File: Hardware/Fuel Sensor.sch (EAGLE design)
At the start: 30 parts, among them IC1 LP2950ACZ-3.3G (TO92), IC2 LTV814, IC3 2N5551, K1 FINDER34-SPDT5, M0 HLK-PM01-AC-DC, M1 WIRELESS-NRF24L01BIG, M2 ARDUINO-PRO-MINI-2ROWSBIG, X1 220Vac, X2 Relay

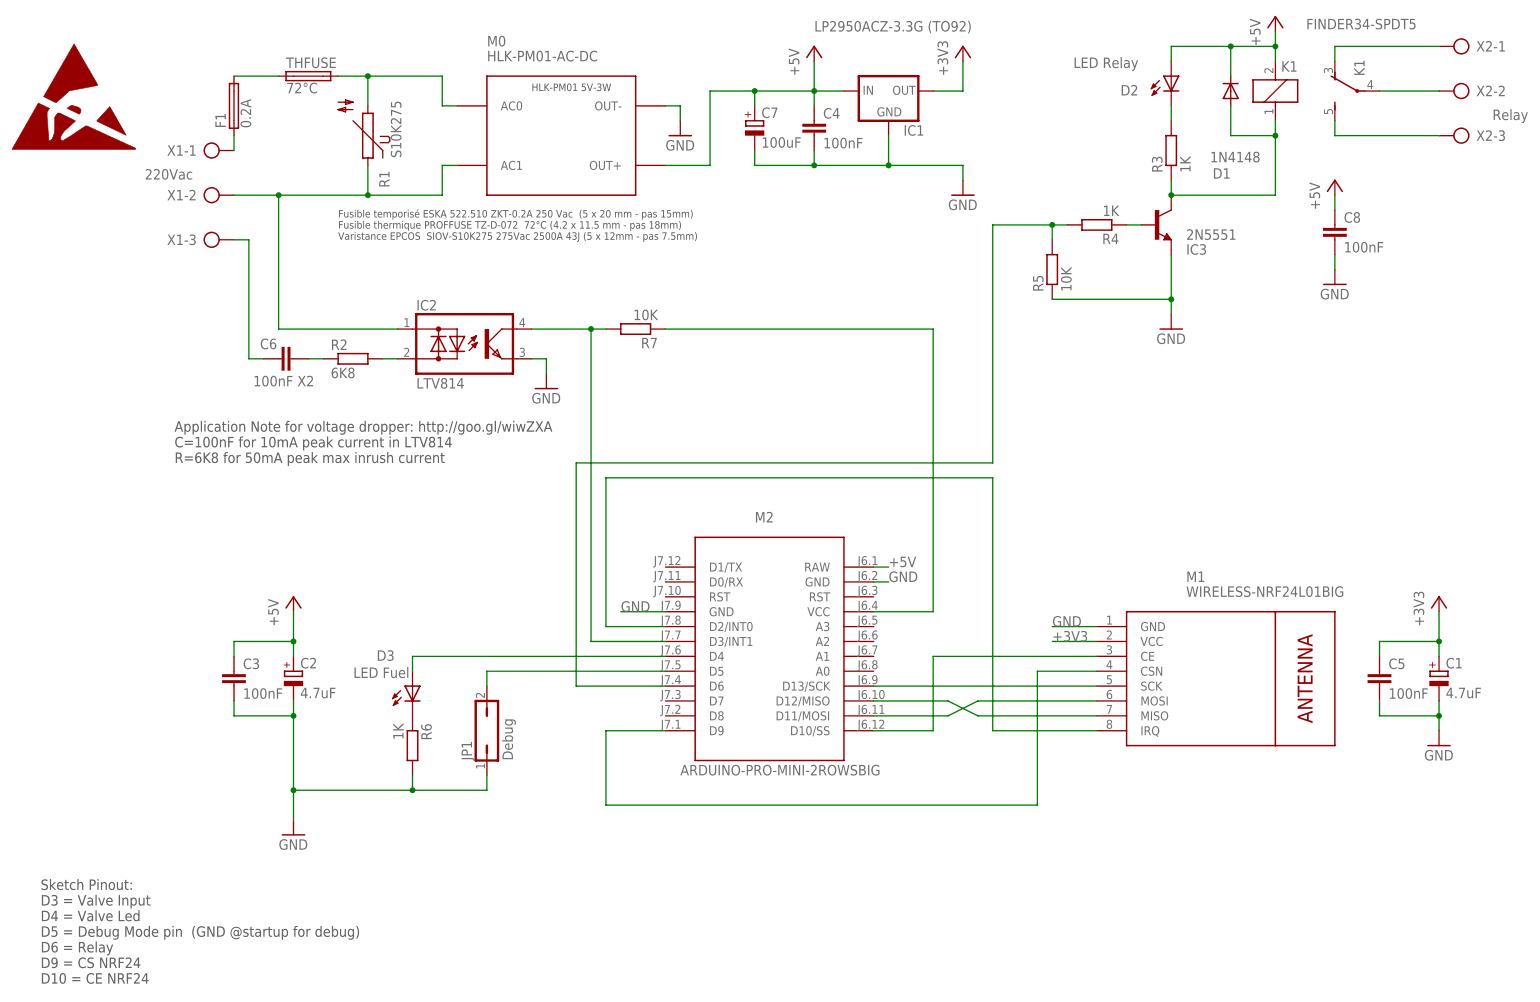
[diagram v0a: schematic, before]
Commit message: Fix Resistor values for LEDs
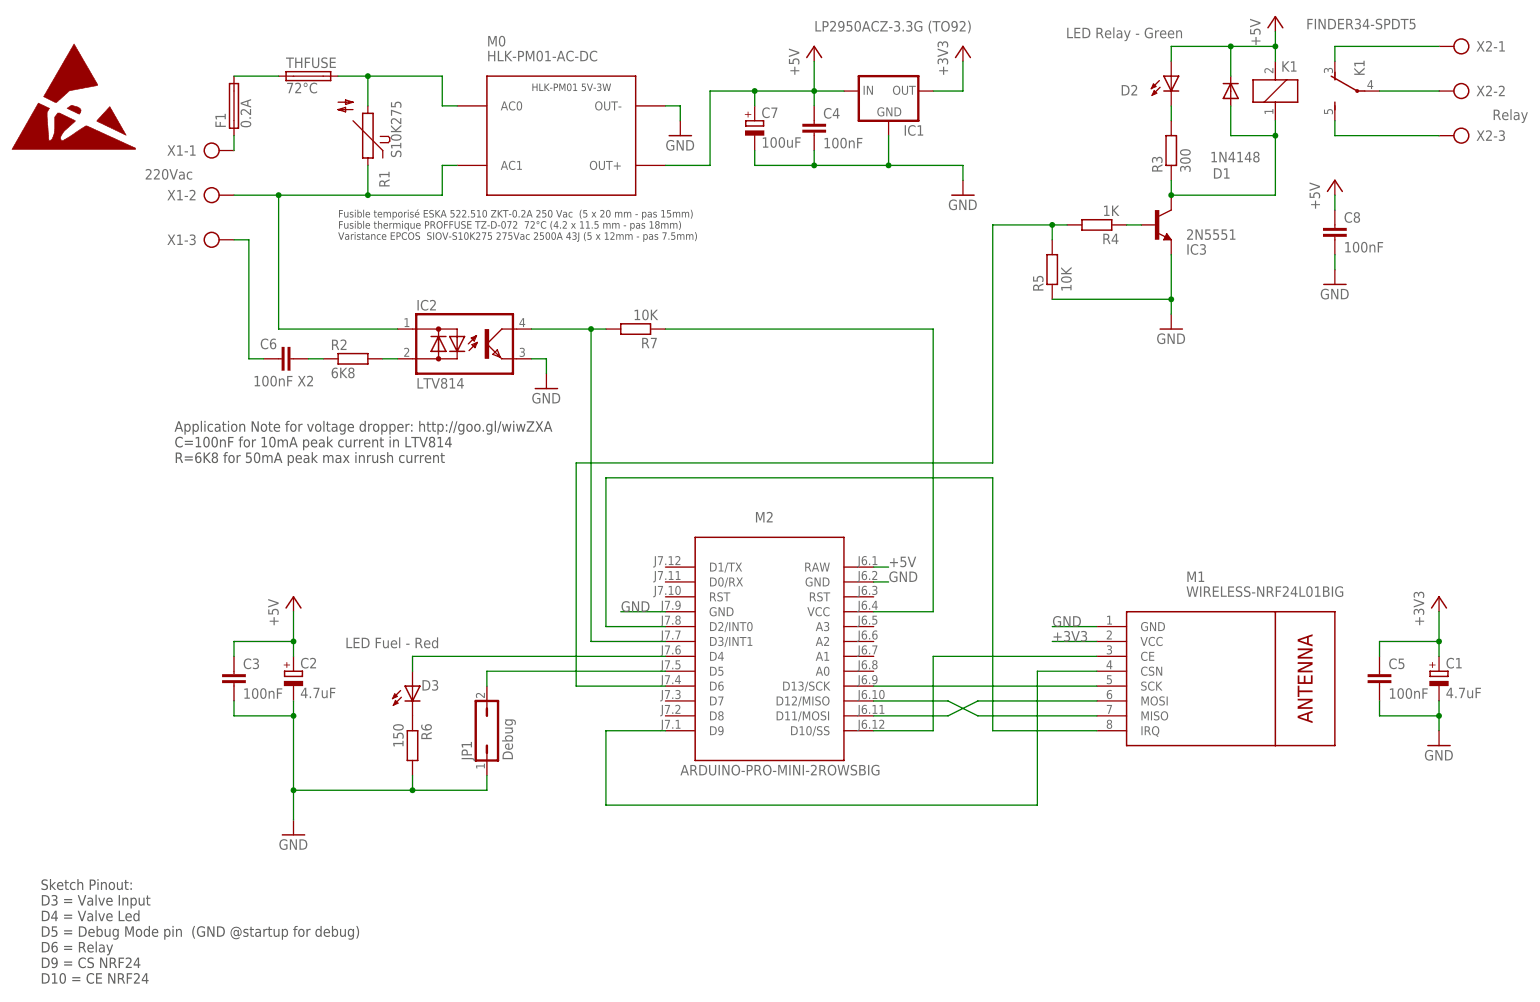
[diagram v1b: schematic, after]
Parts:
- D2: value LED Relay -> LED Relay - Green
- D3: value LED Fuel -> LED Fuel - Red
- R3: value 1K -> 300
- R6: value 1K -> 150
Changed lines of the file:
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@@
 <part name="R5" library="diving91" deviceset="R" device="PMR0.25W" value="10K"/>
 <part name="R4" library="diving91" deviceset="R" device="PMR0.25W" value="1K"/>
-<part name="R3" library="diving91" deviceset="R" device="PMR0.25W" value="1K"/>
+<part name="R3" library="diving91" deviceset="R" device="PMR0.25W" value="300"/>
 <part name="IC3" library="diving91" deviceset="T-NPN" device="T092L" value="2N5551"/>
-<part name="D3" library="diving91" deviceset="LED5MM" device="" value="LED Fuel"/>
-<part name="D2" library="diving91" deviceset="LED5MM" device="" value="LED Relay"/>
-<part name="R6" library="diving91" deviceset="R" device="PMR0.25W" value="1K"/>
+<part name="D3" library="diving91" deviceset="LED5MM" device="" value="LED Fuel - Red"/>
+<part name="D2" library="diving91" deviceset="LED5MM" device="" value="LED Relay - Green"/>
+<part name="R6" library="diving91" deviceset="R" device="PMR0.25W" value="150"/>
 <part name="D1" library="diving91" deviceset="1N4148" device="DO35" value="1N4148"/>
 <part name="C7" library="diving91" deviceset="CPOL-RAD" device="E3-8" value="100uF"/>
@@
 </instance>
 <instance part="D3" gate="G$1" x="81.28" y="66.04" smashed="yes">
-<attribute name="NAME" x="78.232" y="72.136" size="1.778" layer="95" rot="R180"/>
-<attribute name="VALUE" x="80.772" y="69.215" size="1.778" layer="96" rot="R180"/>
+<attribute name="NAME" x="85.852" y="67.056" size="1.778" layer="95" rot="R180"/>
+<attribute name="VALUE" x="85.852" y="74.295" size="1.778" layer="96" rot="R180"/>
 </instance>
 <instance part="D2" gate="G$1" x="210.82" y="170.18" smashed="yes">
 <attribute name="NAME" x="205.232" y="168.656" size="1.778" layer="95" rot="R180"/>
-<attribute name="VALUE" x="205.232" y="173.355" size="1.778" layer="96" rot="R180"/>
+<attribute name="VALUE" x="212.852" y="178.435" size="1.778" layer="96" rot="R180"/>
 </instance>
 <instance part="R6" gate="G$1" x="81.28" y="55.88" rot="R270"/>
